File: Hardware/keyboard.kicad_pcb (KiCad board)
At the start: 2 copper layers, 355.7 x 120 mm, 139 parts

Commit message: Remove Tracks
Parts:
- added C1: 1uF, Capacitor_SMD:C_0805_2012Metric, B.Cu at (310.8, 119.4)
- added C2: 0.1uF, Capacitor_SMD:C_0805_2012Metric, B.Cu at (304.4, 120.2)
- added C3: 0.1uF, Capacitor_SMD:C_0805_2012Metric, B.Cu at (305.9, 115.5)
- added C4: 0.1uF, Capacitor_SMD:C_0805_2012Metric, B.Cu at (310.8, 122.4)
- added C5: 10uF, Capacitor_SMD:C_0805_2012Metric, B.Cu at (315.2, 125.2)
- added F1: 500mA, Fuse:Fuse_1206_3216Metric, B.Cu at (277.2, 153.6)
- added J1: USB2_C_Receptacle, usb-type-c:Mid_Mount-USB_C_HandSoldering, B.Cu at (277.1, 142.6)
- added R1: 10k, Resistor_SMD:R_0805_2012Metric, B.Cu at (275.1, 116.1)
- added R2: 5.1k, Resistor_SMD:R_0805_2012Metric, B.Cu at (270.8, 153.0)
- added R3: 5.1k, Resistor_SMD:R_0805_2012Metric, B.Cu at (283.5, 153.0)
- added R4: 22, Resistor_SMD:R_0805_2012Metric, B.Cu at (278.4, 161.0)
- added R5: 22, Resistor_SMD:R_0805_2012Metric, B.Cu at (275.8, 161.0)
- added R6: 10k, Resistor_SMD:R_0805_2012Metric, B.Cu at (279.5, 116.1)
- added SW1: SW_Push, random-keyboard-parts:SKQG-1155865, B.Cu at (268.2, 117.3)
- added U1: ATmega32U4-AU, Package_QFP:TQFP-44_10x10mm_P0.8mm, B.Cu at (275.0, 209.2)
- added U2: SRV05-4, Package_TO_SOT_SMD:SOT-23-6, B.Cu at (277.1, 156.7)
- added Y1: 16MHz, proj_local:Resonator_SMD_muRata_CSTxExxV-3Pin_3.0x1.1mm_HandSoldering_Compact, B.Cu at (285.0, 132.6)
- moved D_31 7.18 mm to (153.2, 196.8)
- moved D_16 5.12 mm to (152.4, 177.9)
- moved D_59 2.74 mm to (145.3, 234.9)
- moved D_60 2.74 mm to (169.1, 234.9)
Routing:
- net row4: track 114.9 -> 0.00 mm
- net row1: track 110.3 -> 0.00 mm
- net row3: track 110.0 -> 0.00 mm
- net row2: track 108.2 -> 0.00 mm
- net row0: track 100.6 -> 0.00 mm

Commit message: Add Encoders
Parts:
- added SW2: Rotary_Encoder_Switch, Keebio-Parts:RotaryEncoder_EC11, F.Cu at (453.8, 158.4)
- added SW3: Rotary_Encoder_Switch, Keebio-Parts:RotaryEncoder_EC11, F.Cu at (458.7, 177.5)
- added SW4: Rotary_Encoder_Switch, Keebio-Parts:RotaryEncoder_EC11, F.Cu at (463.4, 196.6)
- moved C5 91.5 mm to (224.5, 137.1), turned to 180 degrees
- moved U1 88.3 mm to (233.3, 131.3), turned to 0 degrees
- moved C1 87.2 mm to (224.5, 131.8), turned to 180 degrees
- moved C4 76.0 mm to (237.0, 140.6), turned to 270 degrees
- moved C3 75.5 mm to (230.7, 122.1), turned to 90 degrees
- moved C2 62.2 mm to (242.6, 127.8)
- moved Y1 52.5 mm to (233.6, 122.0), turned to 180 degrees
- moved R6 42.4 mm to (242.1, 135.9), turned to 180 degrees
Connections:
- net Net-(D_15-Pad2) renamed 0row
- net Net-(D_30-Pad2) renamed 1row
- net Net-(D_44-Pad2) renamed 2row
- net col14 renamed 0col
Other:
- board size 355.7 x 120 mm -> 15.2 x 6.3 mm

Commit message: Added PCB Edge Cuts
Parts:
- moved J1 0.28 mm to (277.1, 142.3)
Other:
- board size 15.2 x 6.3 mm -> 358.2 x 123.2 mm
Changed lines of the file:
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@@
   (general
     (thickness 1.6)
-    (drawings 436)
+    (drawings 450)
     (tracks 0)
     (zones 0)
@@
   )
   (module usb-type-c:Mid_Mount-USB_C_HandSoldering (layer B.Cu)
-    (at 277.114 142.621 90)
+    (at 277.114 142.3416 90)
     (fp_text reference J1 (at -1.27 7.62 90) (layer B.SilkS)
       (effects (font (size 0.8 0.8) (thickness 0.15)) (justify mirror))
@@
     )
   )
+  (gr_line (start 269.494 142.3416) (end 130.11781 142.3332) (layer Edge.Cuts) (width 0.2))
+  (gr_line (start 284.734 142.3416) (end 470.3489 142.3332) (layer Edge.Cuts) (width 0.2))
+  (gr_line (start 470.3489 255.2951) (end 332.742904 255.2951) (layer Edge.Cuts) (width 0.2))
+  (gr_arc (start 272.849434 245.547551) (end 269.376506 265.243712) (angle -20.00004079) (layer Edge.Cuts) (width 0.2))
+  (gr_line (start 332.742904 255.2951) (end 276.322447 265.243697) (layer Edge.Cuts) (width 0.2))
+  (gr_line (start 479.3489 151.3332) (end 479.3489 243.744027) (layer Edge.Cuts) (width 0.2))
+  (gr_arc (start 130.11781 151.333201) (end 130.11781 142.3332) (angle -90) (layer Edge.Cuts) (width 0.2))
+  (gr_line (start 185.944746 250.532601) (end 130.11781 250.5326) (layer Edge.Cuts) (width 0.2))
+  (gr_arc (start 130.117809 241.532601) (end 121.117811 241.5326) (angle -90) (layer Edge.Cuts) (width 0.2))
+  (gr_arc (start 470.3489 151.3332) (end 479.3489 151.3332) (angle -90) (layer Edge.Cuts) (width 0.2))
+  (gr_line (start 121.117811 241.5326) (end 121.117811 151.3332) (layer Edge.Cuts) (width 0.2))
+  (gr_line (start 269.376506 265.243712) (end 185.944746 250.532601) (layer Edge.Cuts) (width 0.2))
+  (gr_line (start 479.3489 243.744027) (end 479.3489 246.295101) (layer Edge.Cuts) (width 0.2))
+  (gr_arc (start 470.3489 246.2951) (end 470.3489 255.2951) (angle -90) (layer Edge.Cuts) (width 0.2))
   (gr_line (start 290.09125 244.20465) (end 289.27925 244.34805) (layer Dwgs.User) (width 0.2))
   (gr_line (start 296.17925 239.85285) (end 289.53025 241.02415) (layer Dwgs.User) (width 0.2))

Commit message: Redo Edge Cuts
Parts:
- moved D_36 7.16 mm to (256.3, 212.0)
- moved D_50 7.16 mm to (262.4, 232.4)
- moved D_33 7.16 mm to (200.0, 202.0)
- moved D_4 7.16 mm to (211.3, 165.3)
- moved D_18 7.16 mm to (198.6, 182.5)
- moved D_20 7.16 mm to (236.2, 189.1)
- moved D_35 7.16 mm to (237.5, 208.7)
- moved D_47 7.16 mm to (206.1, 222.5)
- moved D_49 7.16 mm to (243.6, 229.1)
- moved D_6 7.16 mm to (248.8, 172.0)
- moved D_3 7.16 mm to (192.6, 162.0)
- moved D_19 7.16 mm to (217.4, 185.8)
- moved D_21 7.16 mm to (254.9, 192.4)
- moved D_34 7.16 mm to (218.8, 205.4)
- moved D_48 7.16 mm to (224.9, 225.8)
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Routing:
- net D+: track 0.00 -> 11.4 mm
- net D-: track 0.00 -> 9.90 mm
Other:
- board size 358.2 x 123.2 mm -> 352.2 x 117.2 mm

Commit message: Wire USB
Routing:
- net VBUS: track 0.00 -> 24.3 mm, vias 0 -> 2
- net Net-(J1-PadA5): track 0.00 -> 5.87 mm
- net Net-(J1-PadB5): track 0.00 -> 5.37 mm
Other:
- net class PWR added: clearance 0.2, trace_width 0.381, via_dia 0.8, via_drill 0.4
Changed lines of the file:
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@@
     (thickness 1.6)
     (drawings 449)
-    (tracks 18)
+    (tracks 44)
     (zones 0)
     (modules 159)
@@
     (uvia_dia 0.3)
     (uvia_drill 0.1)
-    (add_net +5V)
     (add_net 0col)
     (add_net 0row)
@@
     (add_net ENC2A)
     (add_net ENCB)
-    (add_net GND)
     (add_net "Net-(C1-Pad1)")
     (add_net "Net-(D_1-Pad2)")
@@
     (add_net "Net-(U2-Pad3)")
     (add_net "Net-(U2-Pad4)")
-    (add_net VBUS)
     (add_net col0)
     (add_net col1)
@@
     (add_net row4)
   )
+  (net_class PWR ""
+    (clearance 0.2)
+    (trace_width 0.381)
+    (via_dia 0.8)
+    (via_drill 0.4)
+    (uvia_dia 0.3)
+    (uvia_drill 0.1)
+    (add_net +5V)
+    (add_net GND)
+    (add_net VBUS)
+  )
   (module Keebio-Parts:RotaryEncoder_EC11 (layer F.Cu)
     (at 463.3595 196.596 90)
@@
   (gr_line (start 228.59525 244.11375) (end 229.40625 244.25705) (layer Dwgs.User) (width 0.2))
   (gr_line (start 229.08125 241.35625) (end 228.59525 244.11375) (layer Dwgs.User) (width 0.2))
+  (via (at 274.1168 152.9588) (size 0.8) (drill 0.4) (layers F.Cu B.Cu) (net 89))
+  (segment (start 274.664 151.2368) (end 274.664 152.447747) (width 0.381) (layer B.Cu) (net 89))
+  (segment (start 274.664 152.447747) (end 274.039747 153.072) (width 0.381) (layer B.Cu) (net 89))
+  (via (at 280.53785 152.9528) (size 0.8) (drill 0.4) (layers F.Cu B.Cu) (net 89))
+  (segment (start 280.20904 152.9528) (end 280.53785 152.9528) (width 0.381) (layer B.Cu) (net 89))
+  (segment (start 279.564 151.2368) (end 279.564 152.30776) (width 0.381) (layer B.Cu) (net 89))
+  (segment (start 279.564 152.30776) (end 280.20904 152.9528) (width 0.381) (layer B.Cu) (net 89))
+  (segment (start 274.158947 152.9528) (end 274.039747 153.072) (width 0.381) (layer F.Cu) (net 89))
+  (segment (start 280.53785 152.9528) (end 274.158947 152.9528) (width 0.381) (layer F.Cu) (net 89))
+  (segment (start 279.27321 155.12771) (end 278.5775 154.432) (width 0.381) (layer B.Cu) (net 89))
+  (segment (start 282.79277 155.12771) (end 279.27321 155.12771) (width 0.381) (layer B.Cu) (net 89))
+  (segment (start 283.40451 154.51597) (end 282.79277 155.12771) (width 0.381) (layer B.Cu) (net 89))
+  (segment (start 283.40451 153.07803) (end 283.40451 154.51597) (width 0.381) (layer B.Cu) (net 89))
+  (segment (start 283.03297 152.70649) (end 283.40451 153.07803) (width 0.381) (layer B.Cu) (net 89))
+  (segment (start 281.103535 152.9528) (end 281.349845 152.70649) (width 0.381) (layer B.Cu) (net 89))
+  (segment (start 281.349845 152.70649) (end 283.03297 152.70649) (width 0.381) (layer B.Cu) (net 89))
+  (segment (start 280.53785 152.9528) (end 281.103535 152.9528) (width 0.381) (layer B.Cu) (net 89))
+  (segment (start 279.125 157.5308) (end 278.214 157.5308) (width 0.381) (layer B.Cu) (net 89))
+  (segment (start 279.27321 155.12771) (end 279.27321 157.38259) (width 0.381) (layer B.Cu) (net 89))
+  (segment (start 279.27321 157.38259) (end 279.125 157.5308) (width 0.381) (layer B.Cu) (net 89))
   (segment (start 277.864 152.3368) (end 277.864 151.2368) (width 0.25) (layer B.Cu) (net 91))
   (segment (start 277.319011 152.881789) (end 277.864 152.3368) (width 0.25) (layer B.Cu) (net 91))
@@
   (segment (start 277.364 152.20039) (end 277.364 151.2368) (width 0.25) (layer B.Cu) (net 93))
   (segment (start 276.869002 152.695388) (end 277.364 152.20039) (width 0.25) (layer B.Cu) (net 93))
+  (segment (start 275.864 152.3368) (end 275.864 151.2368) (width 0.25) (layer B.Cu) (net 127))
+  (segment (start 274.4038 153.797) (end 275.864 152.3368) (width 0.25) (layer B.Cu) (net 127))
+  (segment (start 271.7015 153.797) (end 274.4038 153.797) (width 0.25) (layer B.Cu) (net 127))
+  (segment (start 278.864 152.3368) (end 278.864 151.2368) (width 0.25) (layer B.Cu) (net 128))
+  (segment (start 280.3242 153.797) (end 278.864 152.3368) (width 0.25) (layer B.Cu) (net 128))
+  (segment (start 282.5265 153.797) (end 280.3242 153.797) (width 0.25) (layer B.Cu) (net 128))
 )

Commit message: Wire Matrix + Place MCU
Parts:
- moved Y1 95.8 mm to (281.3, 205.0), turned to 90 degrees
- moved C3 94.6 mm to (281.2, 202.1), turned to 0 degrees
- moved C2 92.1 mm to (275.5, 213.8), turned to 270 degrees
- moved R1 83.3 mm to (280.4, 199.2), turned to 90 degrees
- moved U1 83.0 mm to (272.0, 204.7), turned to 270 degrees
- moved SW1 81.6 mm to (295.1, 194.4), turned to 10 degrees
- moved R6 81.6 mm to (267.4, 213.5), turned to 90 degrees
- moved C1 79.4 mm to (271.5, 195.9), turned to 90 degrees
- moved C4 72.5 mm to (262.7, 208.4), turned to 180 degrees
- moved C5 72.1 mm to (266.2, 195.9), turned to 90 degrees
- moved R4 29.1 mm to (270.4, 191.8)
- moved R5 29.0 mm to (268.4, 191.8)
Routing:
- net row4: track 0.00 -> 336.8 mm
- net row2: track 0.00 -> 328.4 mm
- net row1: track 0.00 -> 324.2 mm, vias 0 -> 2
- net row0: track 0.00 -> 321.7 mm, vias 0 -> 2
- net row3: track 0.00 -> 310.8 mm
- net 0col: track 0.00 -> 101.5 mm
- net col12: track 0.00 -> 96.4 mm
- net col10: track 0.00 -> 96.0 mm
- net col13: track 0.00 -> 95.2 mm
- net col11: track 0.00 -> 92.6 mm
- net col1: track 0.00 -> 89.4 mm
- net col9: track 0.00 -> 89.4 mm
- net col2: track 0.00 -> 87.6 mm
- net col4: track 0.00 -> 87.5 mm
- net col7: track 0.00 -> 86.5 mm
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
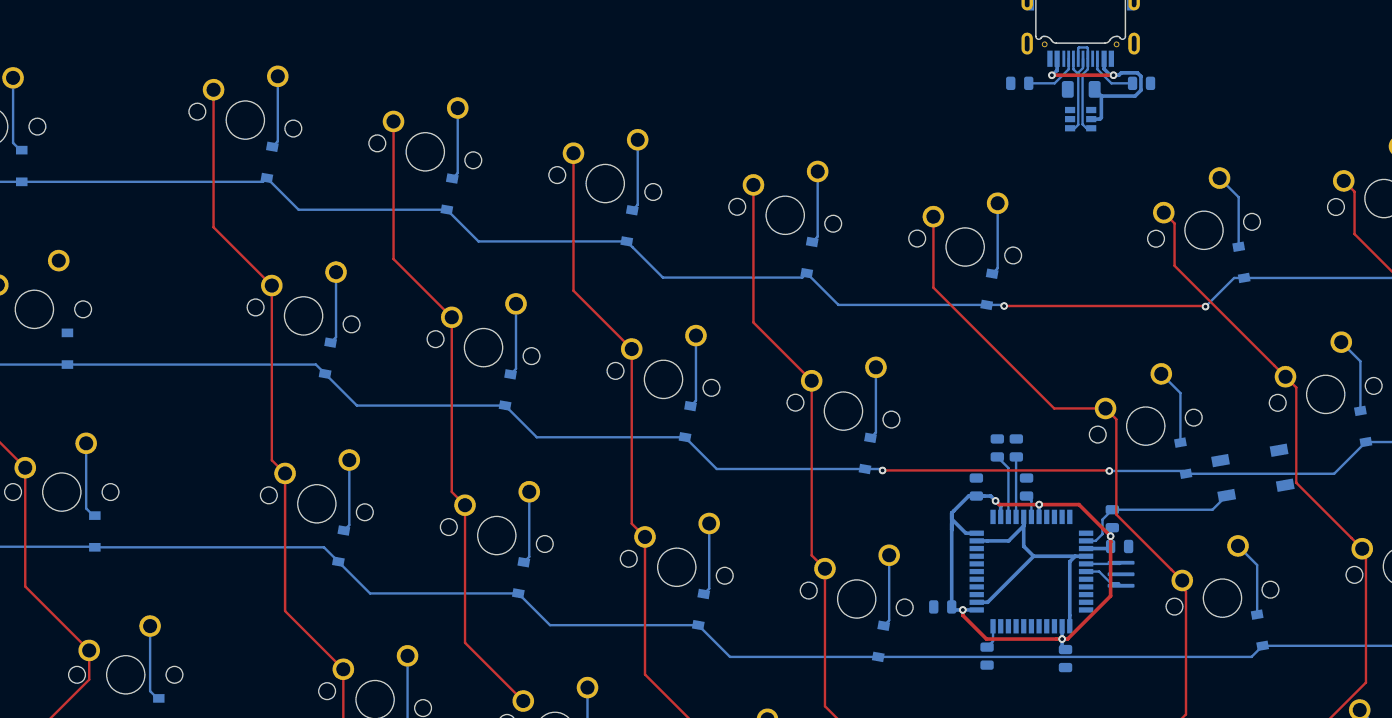
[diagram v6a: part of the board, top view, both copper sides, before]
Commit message: Assign Rows + Cols to pins
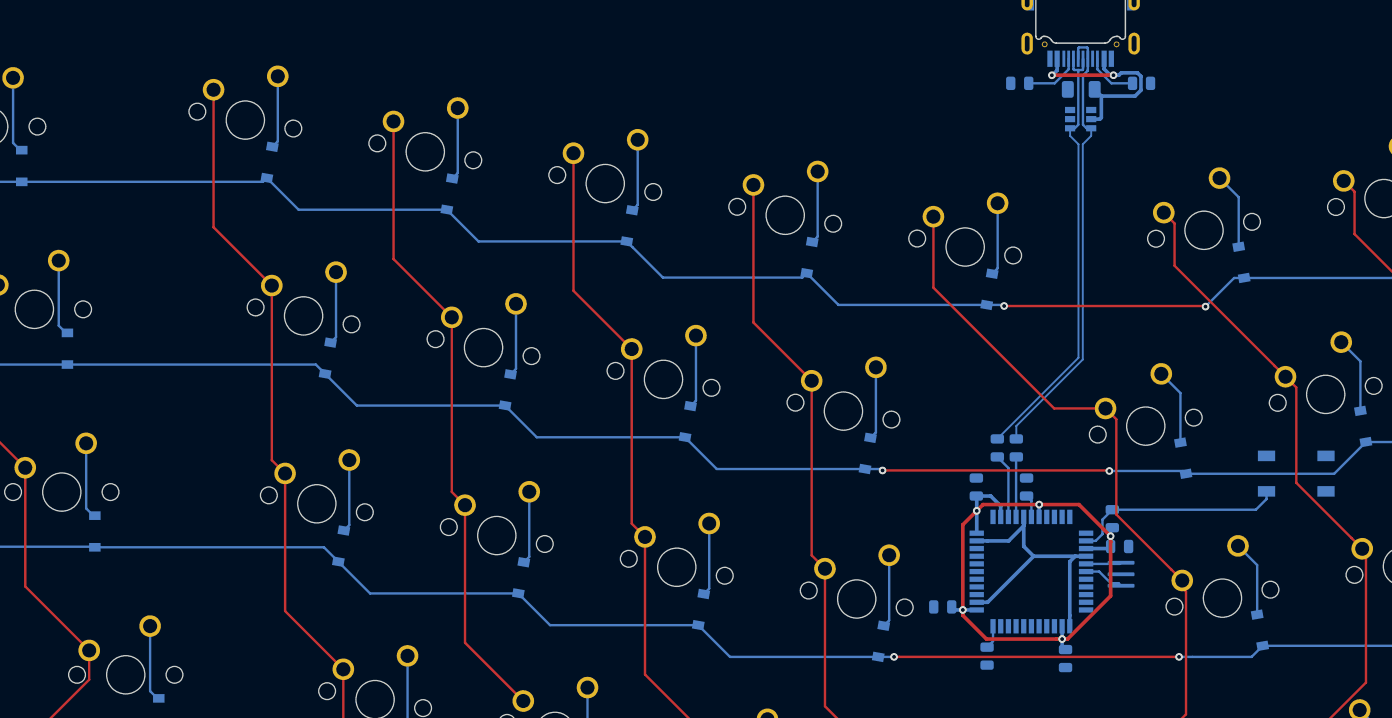
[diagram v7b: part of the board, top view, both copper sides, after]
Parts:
- moved SW1 4.52 mm to (299.6, 194.5), turned to 0 degrees
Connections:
- U1 pad 10: Net-(U1-Pad10) -> col8
- U1 pad 11: Net-(U1-Pad11) -> col9
- U1 pad 12: Net-(U1-Pad12) -> row1
- U1 pad 18: Net-(U1-Pad18) -> col10
- U1 pad 19: Net-(U1-Pad19) -> col11
- U1 pad 20: Net-(U1-Pad20) -> col12
- U1 pad 21: Net-(U1-Pad21) -> col13
- U1 pad 22: Net-(U1-Pad22) -> 0col
- U1 pad 25: Net-(U1-Pad25) -> ENC0A
- U1 pad 26: Net-(U1-Pad26) -> ENC1A
- U1 pad 27: Net-(U1-Pad27) -> ENC2A
- U1 pad 28: Net-(U1-Pad28) -> ENCB
- U1 pad 29: Net-(U1-Pad29) -> col6
- U1 pad 30: Net-(U1-Pad30) -> col5
- U1 pad 31: Net-(U1-Pad31) -> col4
- U1 pad 32: Net-(U1-Pad32) -> col3
- U1 pad 36: Net-(U1-Pad36) -> row4
- U1 pad 37: Net-(U1-Pad37) -> row3
- U1 pad 38: Net-(U1-Pad38) -> row2
- U1 pad 39: Net-(U1-Pad39) -> col2
- U1 pad 40: Net-(U1-Pad40) -> col1
- U1 pad 41: Net-(U1-Pad41) -> col0
- U1 pad 8: Net-(U1-Pad8) -> row0
- U1 pad 9: Net-(U1-Pad9) -> col7
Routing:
- net D-: track 9.90 -> 47.2 mm
- net D+: track 11.4 -> 47.0 mm
- net Net-(D_17-Pad2): track 0.00 -> 8.00 mm
- net Net-(R1-Pad2): track 17.5 -> 22.3 mm
- net +5V: track 71.9 -> 71.2 mm
- net row2: vias 0 -> 2
